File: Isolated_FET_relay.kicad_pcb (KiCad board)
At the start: 2 copper layers, 46.5 x 27 mm, 20 parts, among them P1 CONN_01X05, P2 CONN_01X03, Q1 Q_NMOS_GDS, Q2 Q_NMOS_GDS, U1 Si8751, U2 REG113-XX-SOT23, U3 BGM111

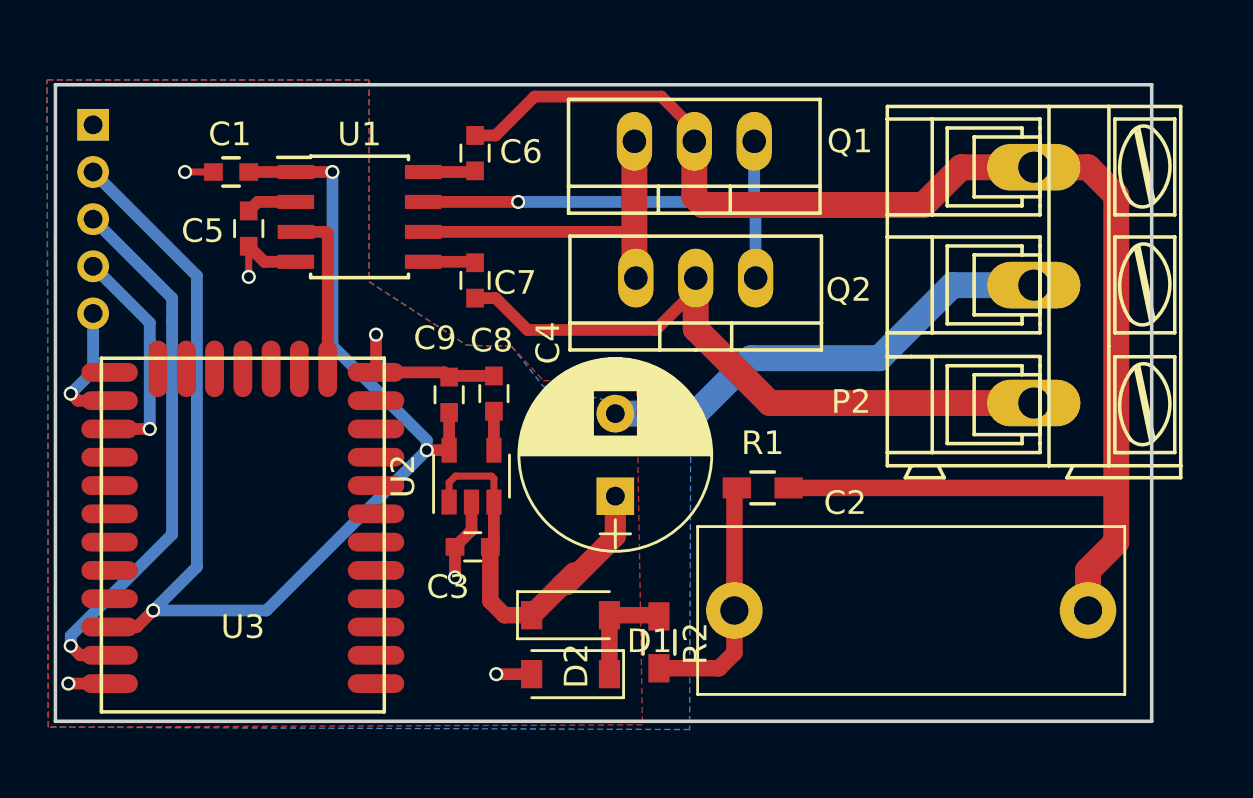
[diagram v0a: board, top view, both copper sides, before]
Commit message: Added gitignore. Created new layout to fit in the box
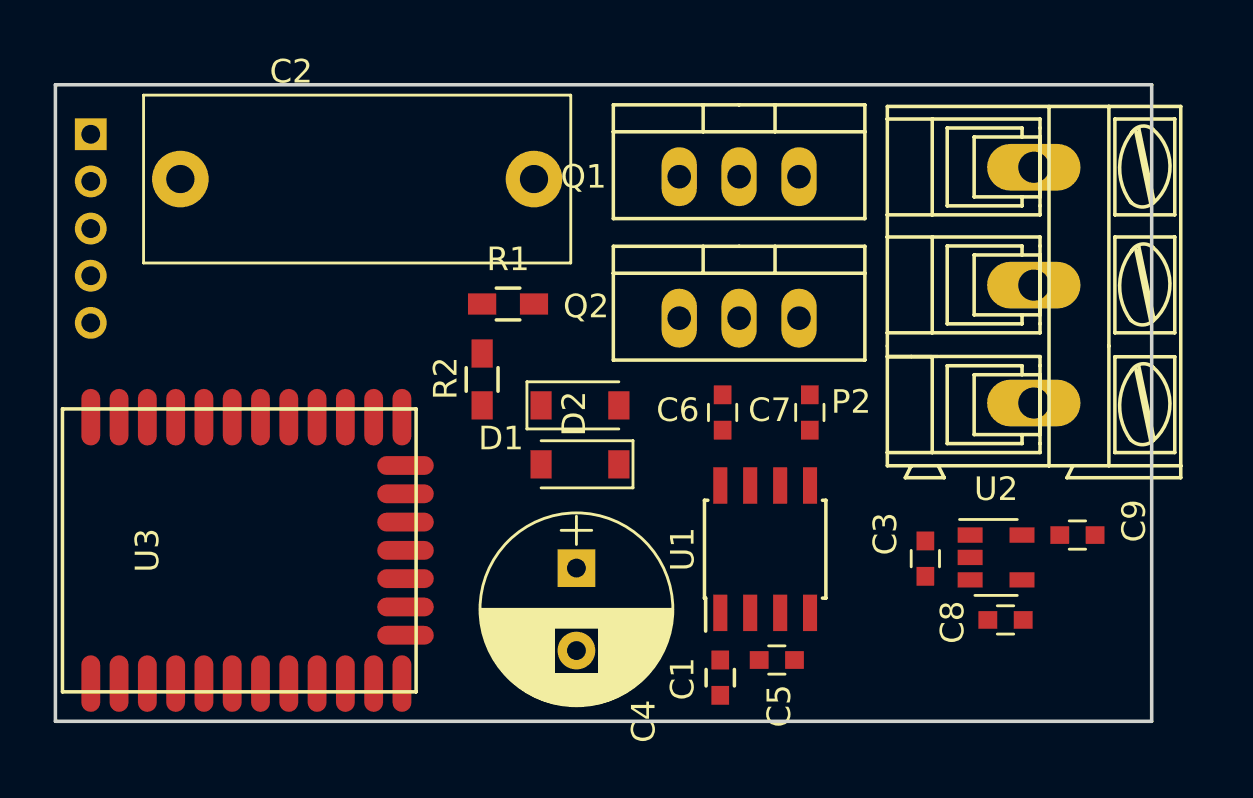
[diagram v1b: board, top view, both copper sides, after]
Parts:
- moved C1 29.8 mm to (169.2, 102.2), turned to 270 degrees
- moved C2 29.8 mm to (146.3, 81.0)
- moved C5 28.9 mm to (171.6, 101.4), turned to 180 degrees
- moved C9 27.3 mm to (184.3, 96.1), turned to 0 degrees
- moved C8 23.7 mm to (181.3, 99.7), turned to 180 degrees
- moved U2 22.5 mm to (180.9, 97.0), turned to 0 degrees
- moved U1 22.2 mm to (171.1, 96.7), turned to 90 degrees
- moved C3 19.2 mm to (177.9, 97.1), turned to 90 degrees
- moved C7 15.3 mm to (173.0, 90.9), turned to 270 degrees
- moved C6 15.2 mm to (169.3, 90.9)
- moved R2 13.4 mm to (159.1, 89.5), turned to 90 degrees
- moved R1 13.3 mm to (160.2, 86.3)
- moved D1 11.4 mm to (163.2, 90.6), turned to 0 degrees
- moved U3 8.57 mm to (142.5, 96.8), turned to 90 degrees
- moved D2 6.41 mm to (163.2, 93.1), turned to 180 degrees
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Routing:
- net /V+: track 64.6 -> 0.00 mm
- net +3V3: track 57.3 -> 0.00 mm, vias 3 -> 0
- net GNDD: track 38.2 -> 0.00 mm, vias 6 -> 0
- net /V-: track 28.9 -> 0.00 mm
- net /DBG_RESET: track 23.1 -> 0.00 mm, vias 1 -> 0
- net /Gate: track 19.9 -> 0.00 mm, vias 1 -> 0
- net +6V: track 17.5 -> 0.00 mm
- net GNDPWR: track 16.6 -> 0.00 mm
- net Net-(C2-Pad1): track 10.5 -> 0.00 mm
- net /DBG_SWD: track 9.59 -> 0.00 mm, vias 1 -> 0
- net /OutputEn: track 7.12 -> 0.00 mm
- net /DBG_CLK: track 5.57 -> 0.00 mm, vias 1 -> 0
- net Net-(D1-Pad1): track 4.47 -> 0.00 mm
- net Net-(C6-Pad2): track 2.22 -> 0.00 mm
- net Net-(C7-Pad2): track 2.22 -> 0.00 mm
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- removed copper zone on B.Cu, net GNDD
- removed copper zone on F.Cu, net GNDD
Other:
- net class High Votlage added: clearance 2.54, trace_width 1, via_dia 3, via_drill 1

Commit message: Created new layout concept
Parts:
- C9: value 10nF -> 100nF
- moved C9 21.5 mm to (163.6, 101.9), turned to 180 degrees
- moved C8 20.6 mm to (160.7, 101.1), turned to 270 degrees
- moved U2 17.5 mm to (163.4, 98.8), turned to 270 degrees
- moved C4 16.5 mm to (179.5, 98.8), turned to 0 degrees
- moved C3 14.9 mm to (163.1, 95.8), turned to 0 degrees
- moved P1 8.00 mm to (142.3, 87.1), turned to 0 degrees
- moved Q2 6.00 mm to (170.0, 80.9)
- moved Q1 5.60 mm to (170.0, 86.5)
- moved D1 3.36 mm to (159.9, 90.8), turned to 180 degrees
- moved R2 1.70 mm to (160.2, 88.2), turned to 180 degrees
- moved C7 1.61 mm to (174.6, 90.7)
- moved D2 1.35 mm to (161.9, 93.1)
- moved C1 1.28 mm to (168.1, 101.5), turned to 180 degrees
- moved P2 1.12 mm to (183.5, 80.0)
- moved C6 0.41 mm to (168.9, 91.0)
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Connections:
- P2 pad 1: /V+ -> /V-
- P2 pad 3: /V- -> /V+
- U3 pad 10: (no net) -> Net-(U3-Pad10)
- U3 pad 11: (no net) -> Net-(U3-Pad11)
- U3 pad 14: (no net) -> Net-(U3-Pad14)
- U3 pad 15: (no net) -> Net-(U3-Pad15)
- U3 pad 16: (no net) -> Net-(U3-Pad16)
- U3 pad 17: (no net) -> Net-(U3-Pad17)
- U3 pad 18: (no net) -> Net-(U3-Pad18)
- U3 pad 19: (no net) -> Net-(U3-Pad19)
- U3 pad 2: (no net) -> Net-(U3-Pad2)
- U3 pad 23: (no net) -> Net-(U3-Pad23)
- U3 pad 24: (no net) -> Net-(U3-Pad24)
- U3 pad 25: (no net) -> Net-(U3-Pad25)
- U3 pad 26: (no net) -> Net-(U3-Pad26)
- U3 pad 27: (no net) -> Net-(U3-Pad27)
- U3 pad 28: (no net) -> Net-(U3-Pad28)
- U3 pad 3: (no net) -> Net-(U3-Pad3)
- U3 pad 4: (no net) -> Net-(U3-Pad4)
- U3 pad 5: (no net) -> Net-(U3-Pad5)
- U3 pad 6: (no net) -> Net-(U3-Pad6)
- U3 pad 7: (no net) -> Net-(U3-Pad7)
- U3 pad 8: (no net) -> Net-(U3-Pad8)
- U3 pad 9: (no net) -> Net-(U3-Pad9)
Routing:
- net +3V3: track 0.00 -> 43.0 mm, vias 0 -> 2
- net /V+: track 0.00 -> 40.1 mm
- net /V-: track 0.00 -> 37.7 mm
- net GNDD: track 0.00 -> 29.0 mm, vias 0 -> 25
- net +6V: track 0.00 -> 28.8 mm, vias 0 -> 1
- net /DBG_CLK: track 0.00 -> 22.0 mm, vias 0 -> 1
- net /DBG_SWD: track 0.00 -> 18.4 mm
- net /OutputEn: track 0.00 -> 18.1 mm, vias 0 -> 2
- net Net-(C2-Pad1): track 0.00 -> 16.9 mm
- net GNDPWR: track 0.00 -> 14.0 mm
- net /Gate: track 0.00 -> 13.9 mm
- net /DBG_RESET: track 0.00 -> 8.75 mm, vias 0 -> 1
- net Net-(D1-Pad1): track 0.00 -> 5.54 mm
- net Net-(C7-Pad2): track 0.00 -> 3.33 mm
- net Net-(C5-Pad2): track 0.00 -> 2.26 mm
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- added copper zone on B.Cu, net GNDD
- added copper zone on F.Cu, net GNDD
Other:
- net class High Votlage: clearance 2.54 -> 2; trace_width 1 -> 0.5
